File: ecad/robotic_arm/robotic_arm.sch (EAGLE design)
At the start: 118 parts, among them J1 (ID,OD)=(2.1,5.5)MM, SW1 5A/28V, Y1 16MHz

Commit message: Replaced Robotic Arm components for those with 3D models.  Also went down to 0402 component size.
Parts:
- removed BATT1: BATTERYPTH_HOLES, PiB:BATTERYPTH_HOLES
- removed S7: TACTILE-SW_500mA/12V, PiB_switches:SWITCH_MOMENTARYSPST-SMD-50MA-12V_L5.2-W5.2
- removed SERVO_INDEX, SERVO_MIDDLE, SERVO_PINKY, SERVO_RING, SERVO_THUMB, SERVO_WRIST: HK15298B, PiB:SERVO-HK15298B
- removed TEMP_INDEX, TEMP_MIDDLE, TEMP_PINKY, TEMP_RING, TEMP_THUMB: TMP36, PiB:TEMPERATURE-SENSOR_TMP36
- removed VREG1: 5A/5V, PiB_ic_power:VREG_MIC29501-5.0_LINEAR_ULDO_5A-5VMIC29501-5.0_5A-5V
- removed VREG3: 1A/3.3V, PiB_ic_power:VREG_TPS76833_ULDO_FAST-TRANSIENT_1A-3.3VTPS76833QDR_1A-3.3V
- added C27: 1000uF/16V, PiB_capacitors:1000UF-POLARIZED_PTH_16V-20%
- added J10, J11, J12, J7, J8, J9: HK15298B, PiB_motors:SERVO_SERVO-PN
- added J2, J3, J4, J5, J6: (no value), PiB_connectors:1X03_MOLEX_PTH_VERT
- added JP2: JUMPER-SMT_2_NO_SILK, PiB_connectors:JUMPER-SMT_2_NO_SILK
- added LIPO1: Molex VERT 2mm pitch, PiB_batteries:BATTERY-CONNECTOR_MOLEX_89400_VERT-MALE_PITCH-2MM
- added S1: 50mA/32V, PiB_switches:SWITCH_MOMENTARY_SPST-NO_SMD_50MA-32V_L4.6-W2.8
- added VREG-MCU: 1A/3.3V, PiB_ic_power:VREG_TPS768XX_ULDO_FAST-TRANSIENT_TPS76833QDR_1A-3.3V
- added VREG-SERVOS: 5A/5V, PiB_ic_power:VREG_MIC29501-5.0_LINEAR_ULDO_5A-5V_MC29501-5.0_5A-5V
- A6: value 2.4GHz/802.11/0.5dBi/3W -> 2.45GHz; device PiB_radio_frequency:ANTENNA_SMD-CHIP_2.4GHZ-0.5DBI-3W -> PiB_radio_frequency:ANTENNA_SMD_CHP-2.45GHZ-0.5DBI-3W
- AVR_ISP: value AVR ISP -> AVRISP; device PiB_connectors:AVR_SPI_PRG_6NS -> PiB_connectors:AVR_SPI_PRG_6_PTH_VERT-MALE
- B1: value Impedence UNBAL/BAL (50Ω/100Ω) -> 50/100
- C1, C10, C12, C14, C16, C19, C22, C26, C3, C4, C47, C48, C49, C5, C50, C51, C52, C54, C6, C63, C7, C79, C8, C83, C85, C93, C96, C98: device PiB_capacitors:0.1UF_SMD-805_50V-10% -> PiB_capacitors:0.1UF_SMD-0402_50V-10%
- C11, C13, C15, C17, C2, C9: value 10uF/20V -> 10uF/16V; device PiB_capacitors:10UF-POLARIZED_SMD-1206_20V-20% -> PiB_capacitors:10UF-POLARIZED_SMD-1206_16V-20%_
- C18, C25, C92: value 10uF/25V -> 10uF/6.3V; device PiB_capacitors:10UF_CER_SMD-805_25V-10% -> PiB_capacitors:10UF_CER_SMD-0402_6.3V-20%
- C20: value 100UF/16V -> 1000uF/16V; device PiB_capacitors:100UF-POLARIZED_SMD_16V-20% -> PiB_capacitors:1000UF-POLARIZED_PTH_16V-20%
- C21, C24: device PiB_capacitors:1UF_SMD-805_25V-10% -> PiB_capacitors:1UF_SMD-0805_25V-10%
- C23, C53, C55, C57, C58: device PiB_capacitors:1UF_SMD-805_25V-10% -> PiB_capacitors:1UF_CER_SMD-0402_25V-10%
- C59, C60: value 12pF/250V -> 12pF/100V; device PiB_capacitors:12PF_SMD-805_250V-5% -> PiB_capacitors:12PF_SMD-0402_100V-5%
- C61: value 22PF/250V -> 22pF/100V; device PiB_capacitors:22PF_SMD-805_250V-5% -> PiB_capacitors:22PF_CER_SMD-0402-100V-5%
- C62: value 0.75PF/100V -> 0.75pF/50V; device PiB_capacitors:0.75PF_SMD-805_100V-33% -> PiB_capacitors:0.75PF_CER_SMD-0402_50V-33%
- C80: value 220uF/16V -> 1000uF/16V; device PiB_capacitors:220UF-POLARIZED_SMD_16V-20% -> PiB_capacitors:1000UF-POLARIZED_PTH_16V-20%
- C81: value 0.1uF/50V -> 0.1uF/35V; device PiB_capacitors:0.1UF_SMD-805_50V-10% -> PiB_capacitors:0.1UF_SMD-0805_35V-10%
- C82, C94, C95, C97: device PiB_capacitors:10UF_CER_SMD-805_25V-10% -> PiB_capacitors:10UF_CER_SMD-0805_25V-10%
- D1: value 1A/50V -> 150mA/75V; device PiB_discrete_semiconductors:DIODE_GENERAL-PURPOSE_SMD_GP_1A-50V -> PiB_discrete_semiconductors:DIODE_GENERAL-PURPOSE_SMD-0402_GP_150MA-75V
- DEMUX1: device PiB:CD74HC4067-SM96_16:1_MUX-DEMUX -> PiB:CD74HC4067-SM96_16:1_MUX-DEMUX_SOP-24_16:1-MUX-DEMUX
- FSR_INDEX, FSR_MIDDLE, FSR_PINKY, FSR_RING, FSR_THUMB: value FSR -> 10K; device PiB:FSR_FORCE-SENSATIVE-RESISTOR_PRESS-SENSOR -> PiB_sensors:FSR_FORCE-SENSATIVE-RESISTOR_PRESS-SENSOR_0530470210_VERT-MALE_PITCH-1.25MM
- J1: value (ID,OD)=(2.1,5.5)MM -> 5A/28V; device PiB_connectors:POWER_JACK-BARREL_ID2.1MM-OD5.5MM -> PiB_connectors:POWER_JACK-BARREL_ID2.1MM-OD5.5MM_PTH_ID2.1MM-OD5.5MM
- JP1: value FTDIPTH-RA -> FTDI; device PiB_connectors:FTDIPTH-RA -> PiB_connectors:FTDI_PTH_RA-MALE
- L1, L2: value 10uH -> 10uH/380mA; device PiB_inductors:10UH_SMD-805_0.5A-0.65OHM-10% -> PiB_inductors:10UH_SMD-0603_0.38A-0.468OHM-10%
- L3: device PiB_leds:LED_SMD-0805_DISCRETE_BLUE -> PiB_leds:LED_SMD-0402_DISCRETE_BLUE
- L4: device PiB_leds:LED_SMD-0805_DISCRETE_GREEN -> PiB_leds:LED_SMD-0402_DISCRETE_GREEN
- L5: device PiB_leds:LED_SMD-0805_DISCRETE_RED -> PiB_leds:LED_SMD-0402_DISCRETE_RED
- MCU: value ATMEGA128RFA1 -> ATMEGA128RFA1_VFQFN-64_NO-EXPOSED-PAD; device PiB_ic_microcontrollers:ATMEGA128RFA1_VFQFN-64_EXPOSED-PAD -> PiB_ic_microcontrollers:ATMEGA128RFA1_VFQFN-64_NO-EXPOSED-PAD
- PWM_DRIVER: device PiB:PCA9685_16-CH_12-BIT_PWM-DRIVER -> PiB:PCA9685_16-CH_12-BIT_PWM-DRIVER_TSSOP-28_PWM-DRIVER_16CH
- R1, R10, R12, R14, R16, R39, R4, R40, R41, R42, R43, R6, R8: value 10KΩ -> 10K; device PiB_resistors:10KΩ_SMD-0805_1/8W-5% -> PiB_resistors:10KΩ_SMD-0402_1/16W-5%
- R11, R13, R15, R5, R7, R9: value 100Ω -> 100; device PiB_resistors:100Ω_SMD-0805_1/8W-5% -> PiB_resistors:100Ω_SMD-0402_1/16W-5%
- R17, R18: value 4.7K -> 10K; device PiB_resistors:4.7KΩ_SMD-0805_1/8W-5% -> PiB_resistors:10KΩ_SMD-0402_1/16W-5%
- R2: value 2KΩ -> 1K; device PiB_resistors:2KΩ_SMD-0805_1/8W-5% -> PiB_resistors:1KΩ_SMD-0402_1/16W-5%
- R3: value 1KΩ -> 1K; device PiB_resistors:1KΩ_SMD-0805_1/8W-5% -> PiB_resistors:1KΩ_SMD-0402_1/16W-5%
- SW1: device PiB_switches:SWITCH_SPDT_VERT_PTH_5A-28V_13L-7W -> PiB_switches:SWITCH_SPDT_VERT_PTH_5A-28V_13L-7W_
- Y1: value 16MHz -> 16 MHz
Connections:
- removed net BATT_+: BATT1.P, J1.PWR, SW1.2
- removed net BATT_-: BATT1.N, J1.GND@1
- new net +: J1.PWR, LIPO1.+, SW1.P
- new net -: J1.GND@1, LIPO1.-
- new net N$12: JP2.2, MCU.AREF
- net 5V: now also J10.VCC, J11.VCC, J12.VCC, J7.VCC, J8.VCC, J9.VCC, VREG-SERVOS.VOUT; no longer SERVO_INDEX.VCC, SERVO_MIDDLE.VCC, SERVO_PINKY.VCC, SERVO_RING.VCC, SERVO_THUMB.VCC, SERVO_WRIST.VCC, VREG1.VOUT
- net AGND: now also J2.1, J3.1, J4.1, J5.1, J6.1; no longer TEMP_INDEX.GND, TEMP_MIDDLE.GND, TEMP_PINKY.GND, TEMP_RING.GND, TEMP_THUMB.GND
- net AVCC: now also J2.3, J3.3, J4.3, J5.3, J6.3, JP2.1; no longer MCU.AREF, TEMP_INDEX.VS, TEMP_MIDDLE.VS, TEMP_PINKY.VS, TEMP_RING.VS, TEMP_THUMB.VS
- net GND: now also AVR_ISP.GND, C27.K, JP1.GND, S1.1, VREG-MCU.!EN, VREG-MCU.GND; no longer AVR_ISP.6, JP1.6, S7.1, VREG3.!EN, VREG3.GND
- net MISO: now also AVR_ISP.MISO; no longer AVR_ISP.1
- net MOSI: now also AVR_ISP.MOSI; no longer AVR_ISP.4
- net N$1: now also J7.SIG; no longer SERVO_WRIST.SIG
- net N$30: now also Y1.XTAL2; no longer Y1.2
- net N$32: now also B1.OUT1; no longer B1.OUT2
- net N$33: now also B1.OUT2; no longer B1.OUT1
- net N$35: now also Y1.XTAL1; no longer Y1.1
- net N$4: now also J8.SIG; no longer SERVO_THUMB.SIG
- net N$41: now also JP1.DTR; no longer JP1.2
- net N$42: now also JP1.CTS; no longer JP1.5
- net N$6: now also J9.SIG; no longer SERVO_INDEX.SIG
- net N$7: now also J10.SIG; no longer SERVO_MIDDLE.SIG
- net N$8: now also J11.SIG; no longer SERVO_RING.SIG
- net N$9: now also J12.SIG; no longer SERVO_PINKY.SIG
- net NGND: now also J10.GND, J11.GND, J12.GND, J7.GND, J8.GND, J9.GND, VREG-SERVOS.GND; no longer SERVO_INDEX.GND, SERVO_MIDDLE.GND, SERVO_PINKY.GND, SERVO_RING.GND, SERVO_THUMB.GND, SERVO_WRIST.GND, VREG1.GND
- net RESET: now also AVR_ISP.RESET, S1.2; no longer AVR_ISP.5, S7.2
- net RX0: now also JP1.TXO; no longer JP1.4
- net SCK: now also AVR_ISP.SCK; no longer AVR_ISP.3
- net TEMP_INDEX: now also J3.2; no longer TEMP_RING.VOUT
- net TEMP_MIDDLE: now also J4.2; no longer TEMP_MIDDLE.VOUT
- net TEMP_PINKY: now also J6.2; no longer TEMP_THUMB.VOUT
- net TEMP_RING: now also J5.2; no longer TEMP_INDEX.VOUT
- net TEMP_THUMB: now also J2.2; no longer TEMP_PINKY.VOUT
- net TX0: now also JP1.RXI; no longer JP1.3
- net VBATT: now also C27.A, SW1.S1, VREG-MCU.VIN, VREG-SERVOS.EN, VREG-SERVOS.VIN; no longer SW1.1, VREG1.EN, VREG1.VIN, VREG3.VIN
- net VCC: now also JP1.VCC, VREG-MCU.VOUT; no longer AVR_ISP.2, JP1.1, VREG3.VOUT
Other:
- note added: "Rev 2"
- note removed: "47K?"
- note removed: "Rev 1"
- moved on the sheet: C22, C24, JP1

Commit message: Start on Rev 2 of robotic arm.  Made minor fixes to Touch Glove Rev 2.
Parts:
- removed ANALOG_BR: 2PT_GND_TIE, PiB_power_symbols:2PT_GND_TIE
- removed C81: 0.1uF/35V, PiB_capacitors:0.1UF_SMD-0805_35V-10%
- removed C82: 10uF/25V, PiB_capacitors:10UF_CER_SMD-0805_25V-10%
- removed D6: 1A/50V, PiB_discrete_semiconductors:DIODE_GENERAL-PURPOSE_SMD_GP_1A-50V
- removed J10, J11, J12, J7, J8, J9: HK15298B, PiB_motors:SERVO_SERVO-PN
- removed R10: 10K, PiB_resistors:10KΩ_SMD-0402_1/16W-5%
- removed R11: 100, PiB_resistors:100Ω_SMD-0402_1/16W-5%
- removed S1: 50mA/32V, PiB_switches:SWITCH_MOMENTARY_SPST-NO_SMD_50MA-32V_L4.6-W2.8
- added C28: 0.1uF/50V, PiB_capacitors:0.1UF_SMD-0402_50V-10%
- added C29: 10uF/6.3V, PiB_capacitors:10UF_CER_SMD-0402_6.3V-20%
- added JP3: JUMPER_SMD_3-PAD_NO_NO-SILK, PiB_connectors:JUMPER_SMD_3-PAD_NO_NO-SILK
- added NOISE_BR1: NET_BRIDGE, PiB_power_symbols:NET_BRIDGE
- added SERVO_INDEX, SERVO_MIDDLE, SERVO_PINKY, SERVO_RING, SERVO_THUMB: HK15298B, PiB_motors:SERVO_HK15298B_PTH_VERT_MALE_2.54MM
- added VREG-ANALOG: MCP1700-1802 1.8V/200mA, PiB_ic_power:VREG_LINEAR_MCP1700_MCP1700T-1802_1.8V-200MA_SOT-23
- AVR_ISP: value AVRISP -> PTH VERT MALE; device PiB_connectors:AVR_SPI_PRG_6_PTH_VERT-MALE -> PiB_connectors:AVR_SPI_PRG_6_PTH_VERT_MALE_2.54MM
- C11, C13, C15, C17, C9: value 10uF/16V -> (none); device PiB_capacitors:10UF-POLARIZED_SMD-1206_16V-20%_ -> PiB_capacitors:100UF-POLARIZED_SMD_25V-20%_DIA5-LS2-H11
- C2: value 10uF/16V -> 0.1uF/50V; device PiB_capacitors:10UF-POLARIZED_SMD-1206_16V-20%_ -> PiB_capacitors:0.1UF_SMD-0402_50V-10%
- C21: device PiB_capacitors:1UF_SMD-0805_25V-10% -> PiB_capacitors:1UF_CER_SMD-0402_25V-10%
- C24: value 1uF/25V -> 0.1uF/50V; device PiB_capacitors:1UF_SMD-0805_25V-10% -> PiB_capacitors:0.1UF_SMD-0402_50V-10%
- C8: value 0.1uF/50V -> 10uF/6.3V; device PiB_capacitors:0.1UF_SMD-0402_50V-10% -> PiB_capacitors:10UF_CER_SMD-0402_6.3V-20%
- FSR_INDEX, FSR_MIDDLE, FSR_PINKY, FSR_RING, FSR_THUMB: device PiB_sensors:FSR_FORCE-SENSATIVE-RESISTOR_PRESS-SENSOR_0530470210_VERT-MALE_PITCH-1.25MM -> PiB_sensors:FORCE-SENSITIVE-RESISTOR_SENSOR_FSR-5MM_0530470210_VERT-MALE_PITCH-1.25MM
- JP1: device PiB_connectors:FTDI_PTH_RA-MALE -> PiB_connectors:FTDI_PTH_VERT_MALE_2.54MM
- JP2: value JUMPER-SMT_2_NO_SILK -> JUMPER_SMD_2-PAD_NO_SILK; device PiB_connectors:JUMPER-SMT_2_NO_SILK -> PiB_connectors:JUMPER_SMD_2-PAD_NO_SILK
- LIPO1: value Molex VERT 2mm pitch -> 7.4V
- MCU: value ATMEGA128RFA1_VFQFN-64_NO-EXPOSED-PAD -> ATMEGA128RFA1; device PiB_ic_microcontrollers:ATMEGA128RFA1_VFQFN-64_NO-EXPOSED-PAD -> PiB_ic_microcontrollers:ATMEGA128RFA1_VFQFN-64_EXPOSED-PAD
- NOISE_BR: value 2PT_GND_TIE -> NET_BRIDGE; device PiB_power_symbols:2PT_GND_TIE -> PiB_power_symbols:NET_BRIDGE
- Y1: device PiB:CRYSTAL_ABM3B_16MHZ_18PF -> PiB_crystals_oscillators_resonators:CRYSTAL_ABM3B_16MHZ_18PF
- renumbered L4 to LED4, L5 to LED5
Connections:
- removed net C10: DEMUX1.C10
- removed net C5: DEMUX1.C5
- removed net C6: DEMUX1.C6
- removed net C7: DEMUX1.C7
- removed net C8: DEMUX1.C8
- removed net C9: DEMUX1.C9
- removed net N$38: ANALOG_BR.P$1, L2.2
- removed net PWM10: PWM_DRIVER.PWM10
- removed net PWM11: PWM_DRIVER.PWM11
- removed net PWM12: PWM_DRIVER.PWM12
- removed net PWM13: PWM_DRIVER.PWM13
- removed net PWM14: PWM_DRIVER.PWM14
- removed net PWM15: PWM_DRIVER.PWM15
- removed net PWM6: PWM_DRIVER.PWM6
- removed net PWM7: PWM_DRIVER.PWM7
- removed net PWM8: PWM_DRIVER.PWM8
- removed net PWM9: PWM_DRIVER.PWM9
- removed net SERVO_WRIST: PWM_DRIVER.PWM5, R10.2, R11.2
- removed net VBATT: C27.A, C80.A, C81.1, C82.1, C95.1, C96.1, C97.1, C98.1, D6.K, D7.K, L3.A, SW1.S1, VREG-MCU.VIN, VREG-SERVOS.EN, VREG-SERVOS.VIN
- new net 3.3V: C19.1, C24.1, C25.1, C52.1, C53.1, C54.1, C55.1, C58.1, C63.1, C92.1, C93.1, D1.K, L1.1, MCU.DEVDD, PWM_DRIVER.VCC, R17.2, R18.2, R43.2, VREG-MCU.VOUT
- new net A1.8V: C28.1, C29.1, JP3.1, VREG-ANALOG.VO
- new net A3.3V: C18.1, C2.1, C22.1, C26.1, C3.1, C4.1, C5.1, C6.1, C7.1, C8.1, DEMUX1.VCC, J2.1, J3.1, J4.1, J5.1, J6.1, JP3.3, L1.2, VREG-ANALOG.VI
- new net VBAT: C27.A, C80.A, C95.1, C96.1, C97.1, C98.1, D7.K, L3.A, SW1.P, VREG-MCU.VIN, VREG-SERVOS.EN, VREG-SERVOS.VIN
- new net VSENSOR: C47.1, C48.1, C49.1, C50.1, C51.1, FSR_INDEX.+, FSR_MIDDLE.+, FSR_PINKY.+, FSR_RING.+, FSR_THUMB.+, JP3.2
- net +: now also SW1.S1; no longer SW1.P
- net -: now also J1.GND_BATTERY; no longer J1.GND@1
- net 5V: now also SERVO_INDEX.VCC, SERVO_MIDDLE.VCC, SERVO_PINKY.VCC, SERVO_RING.VCC, SERVO_THUMB.VCC; no longer C2.A, C8.1, J10.VCC, J11.VCC, J12.VCC, J7.VCC, J8.VCC, J9.VCC
- net AGND: now also B1.GND@5, C2.2, C28.2, C29.2, C61.2, C62.2, C8.2, DEMUX1.C10, DEMUX1.C5, DEMUX1.C6, DEMUX1.C7, DEMUX1.C8, DEMUX1.C9, J2.3, J3.3, J4.3, J5.3, J6.3, L2.2, MCU.AVSS_RFN, MCU.AVSS_RFP, VREG-ANALOG.GND; no longer ANALOG_BR.P$2, J2.1, J3.1, J4.1, J5.1, J6.1
- net AVCC: no longer C18.1, C22.1, C24.1, C26.1, C3.1, C4.1, C47.1, C48.1, C49.1, C5.1, C50.1, C51.1, C6.1, C7.1, DEMUX1.VCC, FSR_INDEX.+, FSR_MIDDLE.+, FSR_PINKY.+, FSR_RING.+, FSR_THUMB.+, J2.3, J3.3, J4.3, J5.3, J6.3, L1.2
- net FSR_INDEX: now also DEMUX1.C1; no longer DEMUX1.C3
- net FSR_PINKY: now also DEMUX1.C4; no longer DEMUX1.C0
- net FSR_RING: now also DEMUX1.C3; no longer DEMUX1.C1
- net FSR_THUMB: now also DEMUX1.C0; no longer DEMUX1.C4
- net GND: now also C59.1, C60.1, J1.GND_JACK, NOISE_BR1.P$1; no longer B1.GND@5, C59.2, C60.2, C61.2, C62.2, C81.2, C82.2, J1.GND@2, L2.1, MCU.AVSS_RFN, MCU.AVSS_RFP, R10.1, S1.1
- net N$1: now also L2.1, NOISE_BR1.P$2; no longer J7.SIG, R11.1
- net N$30: now also C60.2, Y1.XTAL1; no longer C60.1, Y1.XTAL2
- net N$35: now also C59.2, Y1.XTAL2; no longer C59.1, Y1.XTAL1
- net N$4: now also SERVO_THUMB.SIG; no longer J8.SIG
- net N$6: now also SERVO_INDEX.SIG; no longer J9.SIG
- net N$7: now also SERVO_MIDDLE.SIG; no longer J10.SIG
- net N$8: now also SERVO_RING.SIG; no longer J11.SIG
- net N$9: now also SERVO_PINKY.SIG; no longer J12.SIG
- net NGND: now also SERVO_INDEX.GND, SERVO_MIDDLE.GND, SERVO_PINKY.GND, SERVO_RING.GND, SERVO_THUMB.GND; no longer C2.K, C8.2, J10.GND, J11.GND, J12.GND, J7.GND, J8.GND, J9.GND
- net RESET: no longer S1.2
- net SERVO_INDEX: now also PWM_DRIVER.PWM11; no longer PWM_DRIVER.PWM3
- net SERVO_MIDDLE: now also PWM_DRIVER.PWM10; no longer PWM_DRIVER.PWM2
- net SERVO_PINKY: now also PWM_DRIVER.PWM8; no longer PWM_DRIVER.PWM0
- net SERVO_RING: now also PWM_DRIVER.PWM9; no longer PWM_DRIVER.PWM1
- net SERVO_THUMB: now also PWM_DRIVER.PWM12; no longer PWM_DRIVER.PWM4
- net VCC: no longer C19.1, C25.1, C52.1, C53.1, C54.1, C55.1, C58.1, C63.1, C92.1, C93.1, D1.K, D6.A, L1.1, MCU.DEVDD, PWM_DRIVER.VCC, R17.2, R18.2, R43.2, VREG-MCU.VOUT
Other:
- note removed: "CHANGE TO 470 UF"
- note removed: "add diode CD1206-S01575"
- moved on the sheet: C11, C13, C15, C17, C24, C59, C60, C8, C9, L1, L2, SW1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

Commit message: Robotic Arm Rev 2: Complete ToT VR Robo Arm Rev 2.  Ready for fab.
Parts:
- added C30: 0.1uF/50V, PiB_capacitors:0.1UF_SMD-0402_50V-10%
- added FSR_PALM: 10K, PiB_sensors:FORCE-SENSITIVE-RESISTOR_SENSOR_FSR-5MM_0530470210_VERT-MALE_PITCH-1.25MM
- added R10: 10K, PiB_resistors:10KΩ_SMD-0402_1/16W-5%
- C11, C13, C15, C17, C9: value (none) -> 100uF/25V
- LIPO1: value 7.4V -> BATTERY_LIPO_2S_2S_7.4V_PTH-PADS_AWG-18; device PiB_batteries:BATTERY-CONNECTOR_MOLEX_89400_VERT-MALE_PITCH-2MM -> PiB_batteries:BATTERY_LIPO_2S_2S_7.4V_PTH-PADS_AWG-18
- VREG-MCU: value 1A/3.3V -> TPS76833QDR 1A/3.3V
- VREG-SERVOS: value 5A/5V -> MIC29501-5.0 5A/5V
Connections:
- net PB6 renamed RX_LED
- net PB7 renamed TX_LED
- net RX0 renamed RX
- net TX0 renamed TX
- removed net A0: MCU.(ADC0/A0*)PF0
- removed net A1: MCU.(ADC1/A1*)PF1
- removed net A2: MCU.(ADC2/DIG2/A2*)PF2
- removed net A3: MCU.(ADC3/DIG4/A3*)PF3
- removed net A4: MCU.(ADC4/TCK/A4*)PF4
- removed net A5: DEMUX1.SIG, MCU.(ADC5/TMS/A5*)PF5
- removed net A6: MCU.(ADC6/TDO/A6*)PF6
- removed net A7: MCU.(ADC7/TDI/A7*)PF7
- removed net PB4: MCU.(PCINT4/OC2A/D9-PWM9)PB4
- removed net PB5: MCU.(PCINT5/OC1A/D8-PWM8)PB5
- removed net PD4: MCU.(ICP1/D22)PD4
- removed net PD5: MCU.(XCK1/D23)PD5
- removed net PD6: MCU.(T1/D24)PD6
- removed net PD7: MCU.(T0/D25)PD7
- removed net PE2: DEMUX1.S0, MCU.(XCK0/AIN0/D2)PE2
- removed net PE3: MCU.(AIN1/OC3A/D3-PWM3)PE3
- removed net PE4: MCU.(INT4/OC3B/D4-PWM4)PE4
- removed net PE5: MCU.(INT5/OC3C/D5-PWM5)PE5
- removed net PE6: DEMUX1.S1, MCU.(T3/INT6/D6)PE6
- removed net PE7: DEMUX1.S2, MCU.(ICP3/INT7/CLKO/D7)PE7
- removed net PG0: MCU.(DIG3/D16)PG0
- removed net PG1: MCU.(DIG1/D17)PG1
- removed net PG2: MCU.(AMR/D18)PG2
- removed net PG3: MCU.(TOSC2)PG3
- removed net PG4: MCU.(TOSC1)PG4
- removed net PG5: MCU.(OC0B/D19-PWM19)PG5
- removed net RX1: MCU.(INT2/RXD1/D20)PD2
- removed net SSN: DEMUX1.S3, MCU.(PCINT0/SSN/D10)PB0
- removed net TX1: MCU.(INT3/TXD1/D21)PD3
- new net FSR_PALM: DEMUX1.C5, FSR_PALM.-, R10.2
- new net S0: DEMUX1.S0, MCU.(INT4/OC3B/D4-PWM4)PE4
- new net S1: DEMUX1.S1, MCU.(AIN1/OC3A/D3-PWM3)PE3
- new net S2: DEMUX1.S2, MCU.(T3/INT6/D6)PE6
- new net S3: DEMUX1.S3, MCU.(INT5/OC3C/D5-PWM5)PE5
- new net SIG: DEMUX1.SIG, MCU.(ADC2/DIG2/A2*)PF2
- net AGND: now also C30.2, R10.1; no longer DEMUX1.C5
- net VSENSOR: now also C30.1, FSR_PALM.+
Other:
- note removed: "A0/0 --> SIG_PIN of DEMUX"
- note removed: "D10"
- note removed: "D10 --> S3 of DEMUX"
- note removed: "D2"
- note removed: "D2 --> S0 of DEMUX"
- note removed: "D6"
- note removed: "D6 --> S1 of DEMUX"
- note removed: "D7"
- note removed: "D7 --> S2 of DEMUX"
- note removed: "I2C ADDR: x40"
- note removed: "NEED TO FULLY DEFINE THE SERVO DEVICE"
- note removed: "TODO: LOTS OF VIAS"
- moved on the sheet: C79

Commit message: Rev 3: Robotic Arm.  Fix mistake with A3.3V not connected to ATMEGA128RFA1 EVDD (pin 59) which may be affecting the bootload process.
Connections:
- net N$12 renamed AREF
- removed net AVCC: C23.1, C85.1, JP2.1, MCU.EVDD
- removed net VCC: JP1.VCC
- net A3.3V: now also C23.1, C85.1, MCU.EVDD
- net VSENSOR: now also JP2.1
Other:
- note added: "Rev 3"
- note removed: "Rev 2"
- moved on the sheet: D1, JP2, R43

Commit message: Updated aesthetics of robotic arm board.  Changed orientation.
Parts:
- removed J2, J3, J4, J5, J6: (no value), PiB_connectors:1X03_MOLEX_PTH_VERT
- removed L3: BLUE, PiB_leds:LED_SMD-0402_DISCRETE_BLUE
- removed LED4: GREEN, PiB_leds:LED_SMD-0402_DISCRETE_GREEN
- removed LED5: RED, PiB_leds:LED_SMD-0402_DISCRETE_RED
- added LED1: BLUE, PiB_leds:LED_SMD-0402_DISCRETE_BLUE
- added RX_LED: RED, PiB_leds:LED_SMD-0402_DISCRETE_RED
- added TEMP_INDEX, TEMP_MIDDLE, TEMP_PINKY, TEMP_RING, TEMP_THUMB: TMP36, PiB_sensors:TEMPERATURE-SENSOR_TMP36_TMP36_PTH_VERT
- added TX_LED: GREEN, PiB_leds:LED_SMD-0402_DISCRETE_GREEN
- LIPO1: value BATTERY_LIPO_2S_2S_7.4V_PTH-PADS_AWG-18 -> LIPO 2S
- R17, R18: value 10K -> 4.7K; device PiB_resistors:10KΩ_SMD-0402_1/16W-5% -> PiB_resistors:4.7KΩ_SMD-0402_1/16W-5%
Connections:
- removed net N$42: JP1.CTS
- net A3.3V: now also TEMP_INDEX.VCC, TEMP_MIDDLE.VCC, TEMP_PINKY.VCC, TEMP_RING.VCC, TEMP_THUMB.VCC; no longer J2.1, J3.1, J4.1, J5.1, J6.1
- net AGND: now also TEMP_INDEX.GND, TEMP_MIDDLE.GND, TEMP_PINKY.GND, TEMP_RING.GND, TEMP_THUMB.GND; no longer J2.3, J3.3, J4.3, J5.3, J6.3
- net N$2: now also LED1.K; no longer L3.K
- net N$3: now also TX_LED.K; no longer LED4.K
- net N$5: now also RX_LED.K; no longer LED5.K
- net RX_LED: now also RX_LED.A; no longer LED5.A
- net TEMP_INDEX: now also TEMP_INDEX.SIG; no longer J3.2
- net TEMP_MIDDLE: now also TEMP_MIDDLE.SIG; no longer J4.2
- net TEMP_PINKY: now also TEMP_PINKY.SIG; no longer J6.2
- net TEMP_RING: now also TEMP_RING.SIG; no longer J5.2
- net TEMP_THUMB: now also TEMP_THUMB.SIG; no longer J2.2
- net TX_LED: now also TX_LED.A; no longer LED4.A
- net VBAT: now also LED1.A; no longer L3.A
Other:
- note removed: "CHECK THESE FOR ACCURACY"
- note removed: "NOTES: Add more spots for another vibe motor?"
- moved on the sheet: A6, AVR_ISP, B1, C1, C10, C11, C12, C13, C14, C15, C16, C17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

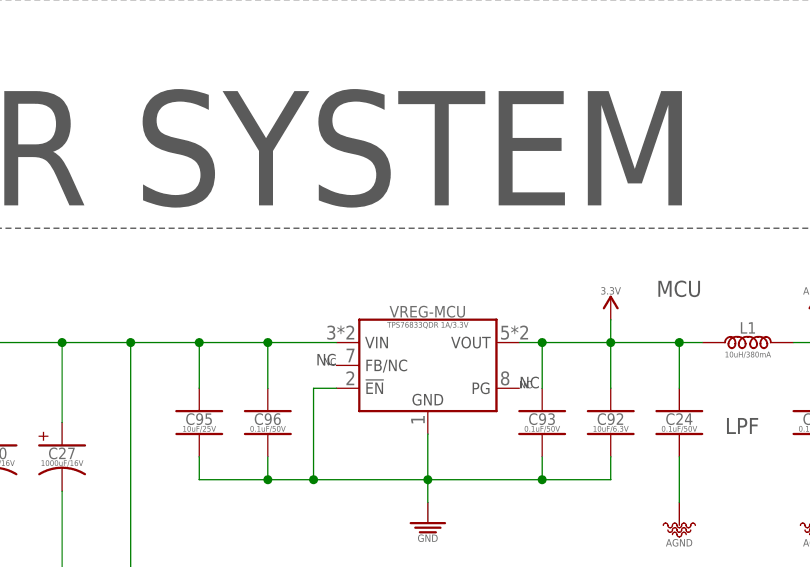
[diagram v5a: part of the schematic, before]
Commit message: Rev 3: Changes to robotic and and touch glove to fix inconsistencies and errors from Rev 2.
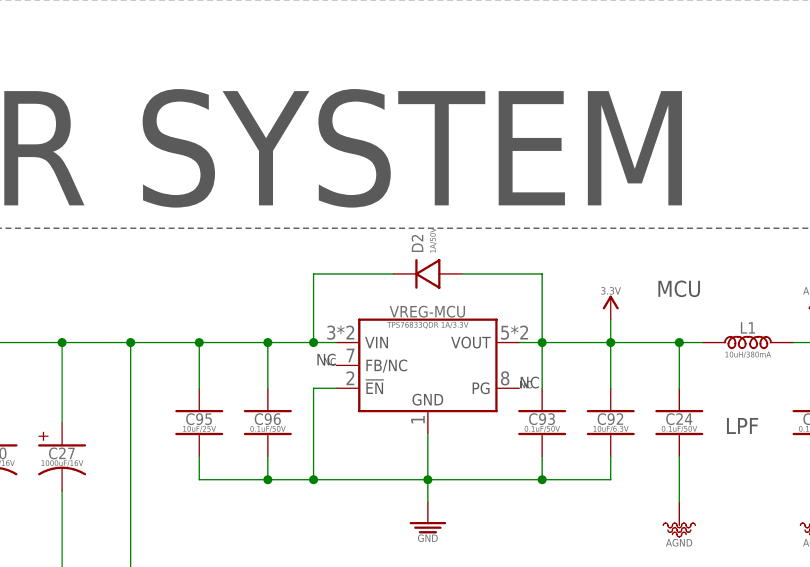
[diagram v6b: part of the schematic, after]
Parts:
- added D2: 1A/50V, PiB_discrete_semiconductors:DIODE_GENERAL-PURPOSE_SMD_GP_1A-50V
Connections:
- net 3.3V: now also D2.A
- net VBAT: now also D2.K
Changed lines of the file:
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@@
 <setting verticaltext="up"/>
 </settings>
-<grid distance="0.1" unitdist="inch" unit="inch" style="lines" multiple="1" display="yes" altdistance="0.05" altunitdist="inch" altunit="inch"/>
+<grid distance="0.1" unitdist="inch" unit="inch" style="lines" multiple="1" display="no" altdistance="0.05" altunitdist="inch" altunit="inch"/>
 <layers>
 <layer number="1" name="Top" color="4" fill="1" visible="no" active="no"/>
@@
 <part name="U$19" library="PiB_power_symbols" deviceset="A3.3V" device=""/>
 <part name="SUPPLY41" library="PiB_power_symbols" deviceset="VSENSOR" device=""/>
+<part name="D2" library="PiB_discrete_semiconductors" deviceset="DIODE_GENERAL-PURPOSE" device="_SMD_GP_1A-50V" package3d_urn="urn:adsk.eagle:package:2939213/1" value="1A/50V"/>
 </parts>
 <sheets>
@@
 <instance part="U$19" gate="G$1" x="187.96" y="330.2" smashed="yes"/>
 <instance part="SUPPLY41" gate="G$1" x="198.12" y="330.2" smashed="yes"/>
+<instance part="D2" gate="G$1" x="252.73" y="190.5" smashed="yes" rot="R90">
+<attribute name="NAME" x="253.492" y="192.786" size="1.27" layer="95" font="vector" ratio="10" rot="R90"/>
+<attribute name="VALUE" x="254.254" y="192.786" size="0.635" layer="96" font="vector" ratio="10" rot="R90" align="top-left"/>
+</instance>
 </instances>
 <busses>
@@
 <wire x1="281.94" y1="177.8" x2="281.94" y2="182.88" width="0.1524" layer="91"/>
 <junction x="281.94" y="182.88"/>
+<pinref part="D2" gate="G$1" pin="A"/>
+<wire x1="257.81" y1="190.5" x2="266.7" y2="190.5" width="0.1524" layer="91"/>
+<wire x1="266.7" y1="190.5" x2="266.7" y2="182.88" width="0.1524" layer="91"/>
 </segment>
 </net>
@@
 <junction x="233.68" y="142.24"/>
 <pinref part="VREG-MCU" gate="G$1" pin="VIN"/>
-<wire x1="243.84" y1="182.88" x2="236.22" y2="182.88" width="0.1524" layer="91"/>
+<wire x1="243.84" y1="182.88" x2="241.3" y2="182.88" width="0.1524" layer="91"/>
 <pinref part="VREG-SERVOS" gate="G$1" pin="VIN"/>
 <pinref part="VREG-SERVOS" gate="G$1" pin="EN"/>
+<wire x1="241.3" y1="182.88" x2="236.22" y2="182.88" width="0.1524" layer="91"/>
 <wire x1="243.84" y1="139.7" x2="243.84" y2="142.24" width="0.1524" layer="91"/>
 <junction x="243.84" y="142.24"/>
@@
 <pinref part="SW1" gate="G$1" pin="P"/>
 <wire x1="185.42" y1="182.88" x2="193.04" y2="182.88" width="0.1524" layer="91"/>
-</segment>
-</net>
+<pinref part="D2" gate="G$1" pin="K"/>
+<wire x1="250.19" y1="190.5" x2="241.3" y2="190.5" width="0.1524" layer="91"/>
+<wire x1="241.3" y1="190.5" x2="241.3" y2="182.88" width="0.1524" layer="91"/>
+<junction x="241.3" y="182.88"/>
+</segment>
+</net>
